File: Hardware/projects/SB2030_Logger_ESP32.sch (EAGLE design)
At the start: 91 parts, among them IC1 MPU6050, T2 S8050, T3 S8050, T4 S8050, U1 ESP32-WROOM-32E, U2 TJA1051T/3, U3 AMS1117-5.0, U4 AMS1117-3.3, U5 SN65C1168PWR, X1 1751280

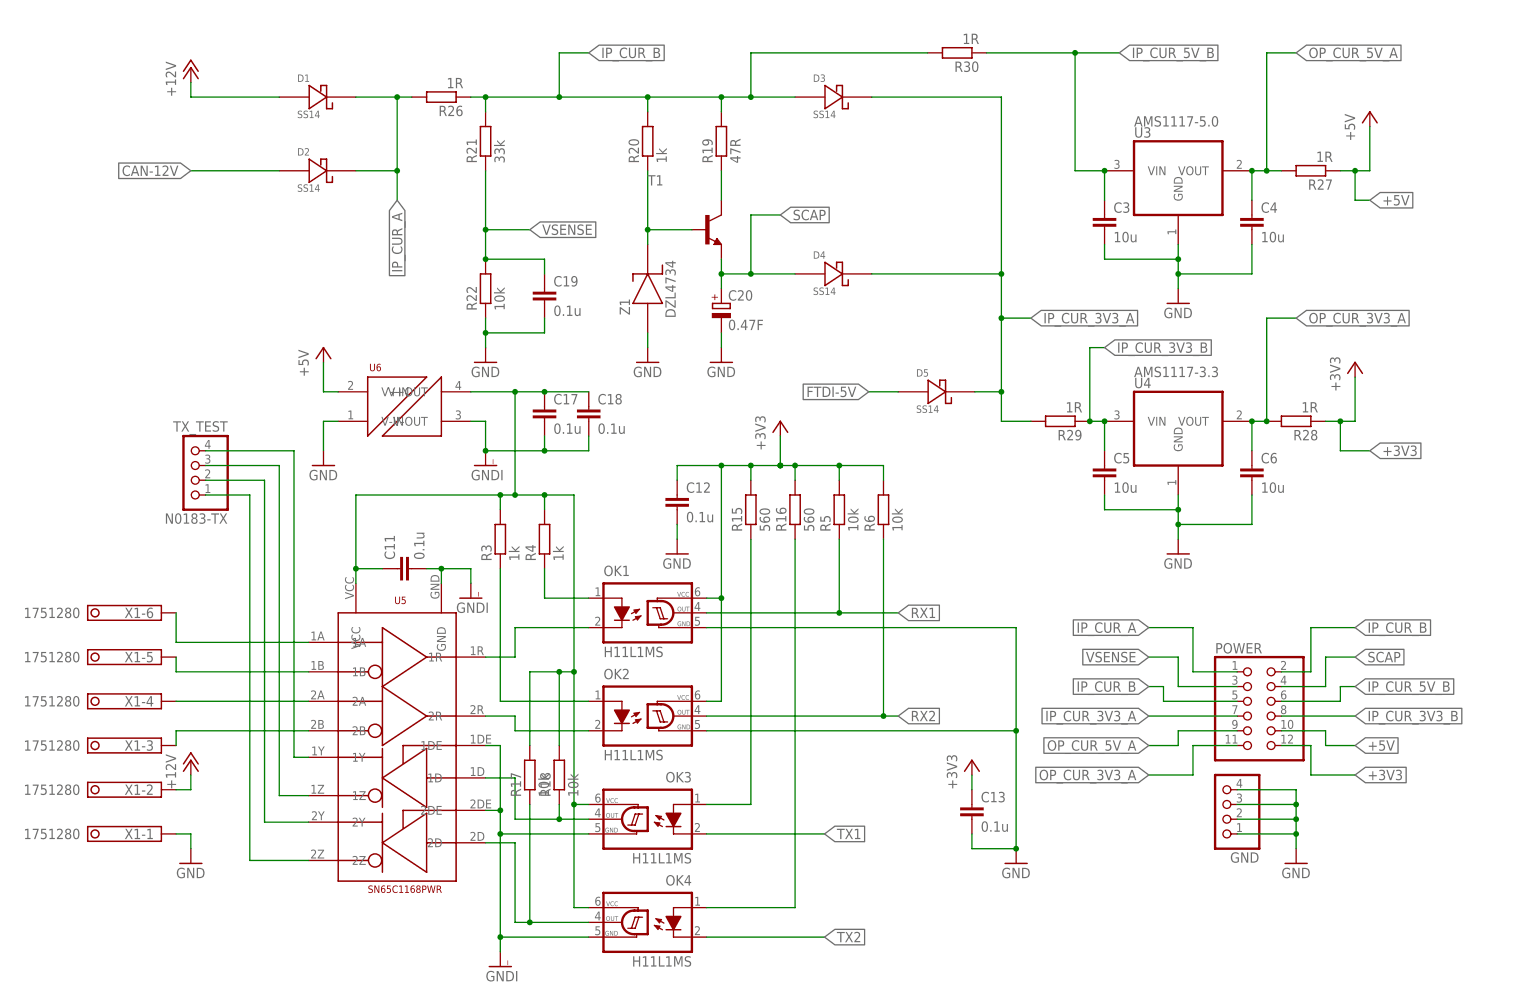
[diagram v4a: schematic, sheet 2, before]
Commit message: Updates to logger schematic and board layout.
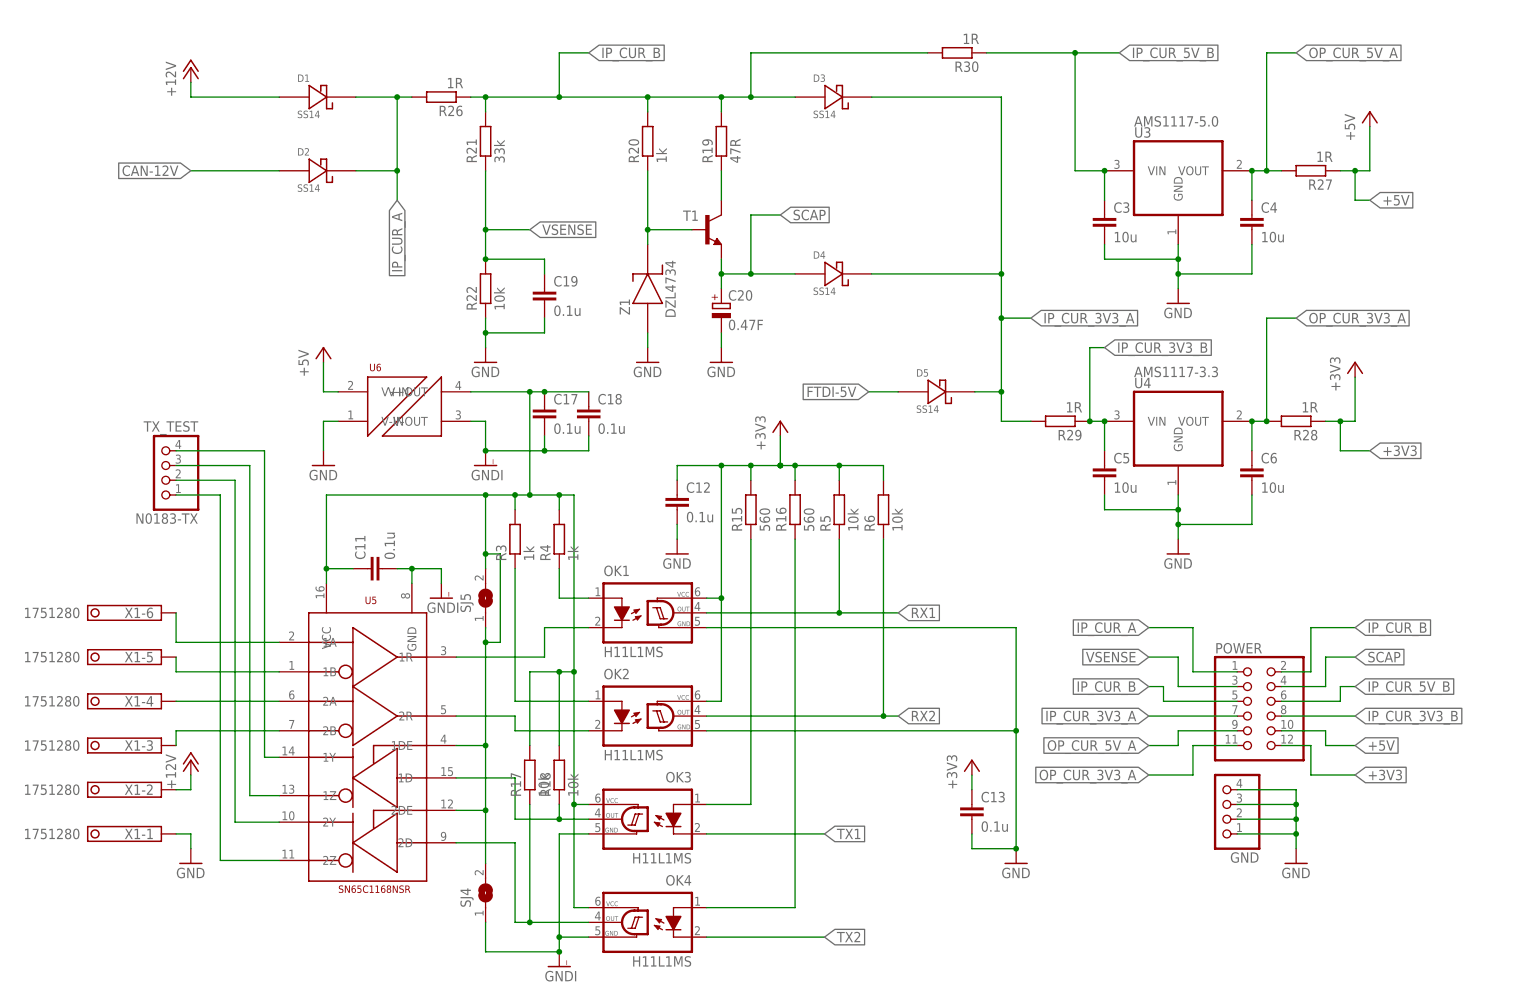
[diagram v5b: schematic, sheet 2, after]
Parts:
- removed SJ2, SJ3: (no value), jumper:SJ
- added C21: 10u, rcl:C-EUC0805
- added C22: 0.1u, rcl:C-EUC0805
- added SJ4, SJ5: (no value), jumper:SJ
- U5: value SN65C1168PWR -> SN65C1168NSR
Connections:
- net +3V3: now also C21.1, C22.1
- net GND: now also C21.2, C22.2
- net GNDI: now also SJ4.1; no longer U5.1DE, U5.2DE
- net N$10: no longer SJ3.1, SJ3.2
- net N$21: now also SJ4.2, SJ5.1, SJ5.2, U5.1DE, U5.2DE
- net N$22: no longer SJ2.1, SJ2.2
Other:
- moved on the sheet: C11, N0183-TX, R3, R4, U5

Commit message: Updates to design for WIBL, board and schematic, to match new SMPS integration, and other small fixes for layout of power input, and super-capacitor charging circuit.
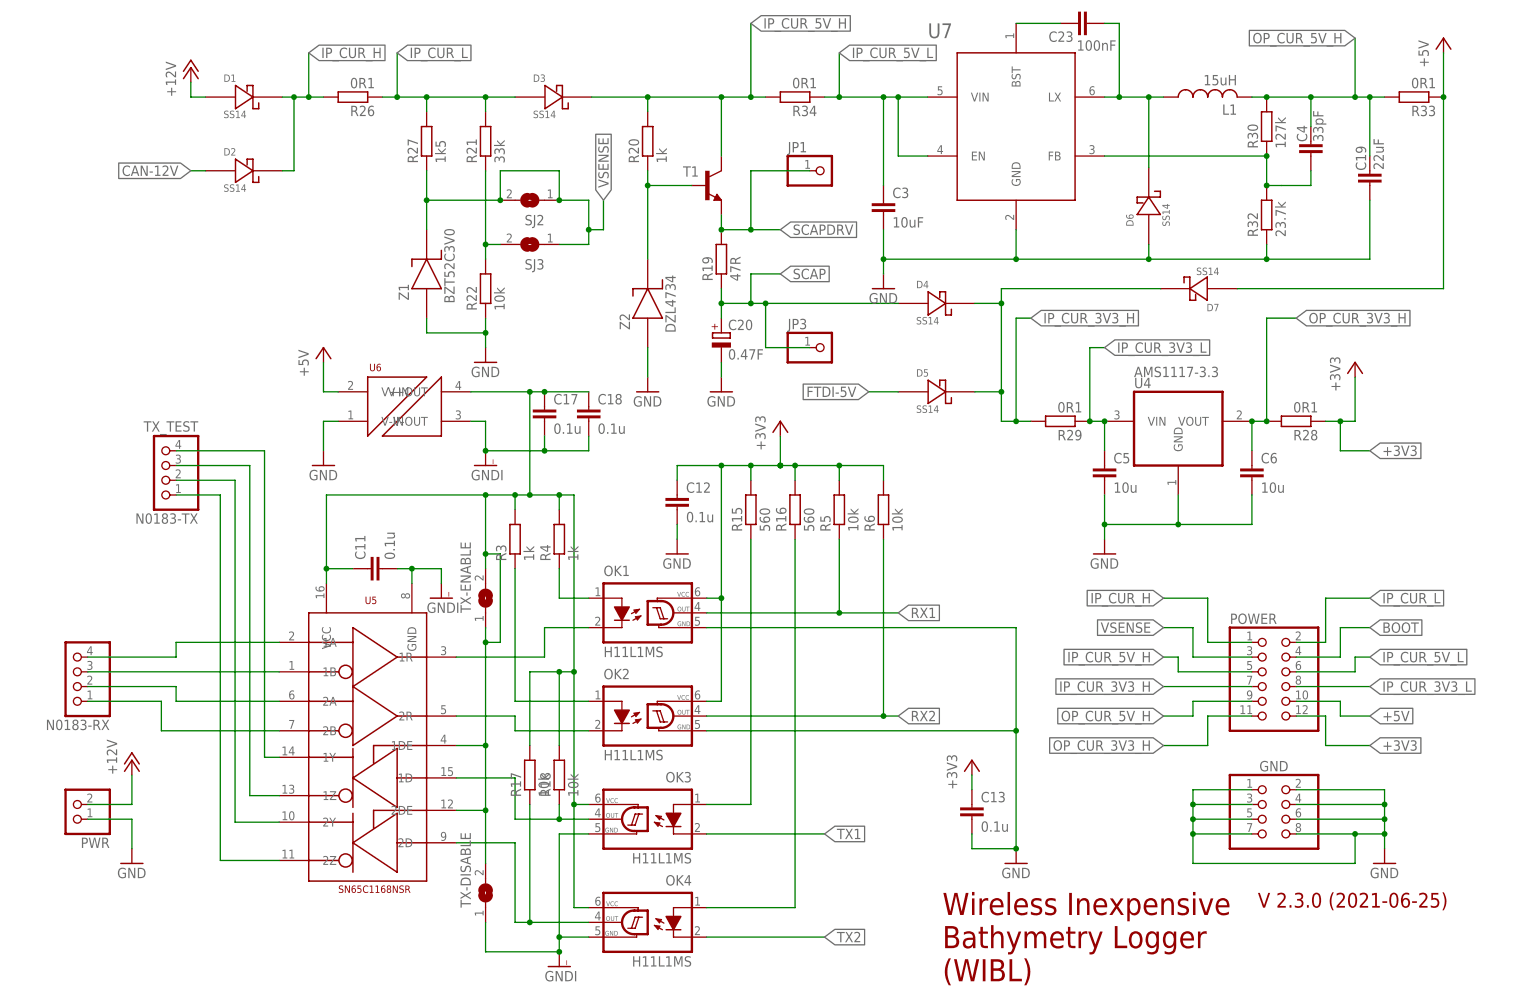
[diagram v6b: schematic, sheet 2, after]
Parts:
- removed C8: 0.1u, rcl:C-EUC0805
- removed U3: AMS1117-5.0, burr-brown:REG1117
- removed X1: 1751280, con-phoenix-350:1751280
- added C23: 100nF, sb2030_logger:C0402
- added D6, D7: SS14, sb2030_logger:SS14
- added JP1, JP3: (no value), pinhead:PINHD-1X1
- added L1: 15uH, sb2030_logger:MWSA0603S
- added N0183-RX: (no value), pinhead:PINHD-1X4
- added PWR: (no value), pinhead:PINHD-1X2
- added R32: 23.7k, rcl:R-EU_R0603
- added R33, R34: 0R1, rcl:R-EU_R0603
- added R35: 47k, rcl:R-EU_R0805
- added SJ2, SJ3: (no value), jumper:SJ
- added U7: (no value), sb2030_logger:BL9352A
- added Z2: DZL4734, sb2030_logger:DZL4734
- C19: value 0.1u -> 22uF; device rcl:C-EUC0805 -> rcl:C-EUC0603
- C3: value 10u -> 10uF; device rcl:C-EUC0805 -> rcl:C-EUC1206
- C4: value 10u -> 33pF; device rcl:C-EUC0805 -> rcl:C-EUC0603
- C7: value 0.1u -> 1uF
- GND: device pinhead:PINHD-1X4 -> pinhead:PINHD-2X4
- R26, R28, R29: value 1R -> 0R1; device rcl:R-EU_R0805 -> rcl:R-EU_R0603
- R27: value 1R -> 1k5
- R30: value 1R -> 127k; device rcl:R-EU_R0805 -> rcl:R-EU_R0603
- Z1: value DZL4734 -> BZT52C3V0; device sb2030_logger:DZL4734 -> sb2030_logger:BZT52C3V0
- renumbered SJ4 to TX-DISABLE, SJ5 to TX-ENABLE
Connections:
- net IP_CUR_3V3_B renamed IP_CUR_3V3_L
- net IP_CUR_A renamed IP_CUR_H
- net OP_CUR_3V3_A renamed OP_CUR_3V3_H
- removed net IP_CUR_3V3_A: D3.K, D4.K, D5.K, POWER.7, R29.2
- removed net IP_CUR_5V_B: C3.1, POWER.6, R30.1, U3.VIN
- removed net IP_CUR_B: D3.A, POWER.2, POWER.5, R19.2, R20.2, R21.2, R26.1, R30.2
- removed net N$12: C8.1, T2.C, U1.GPIO0/BOOT
- removed net OP_CUR_5V_A: C4.1, POWER.9, R27.2, U3.VOUT
- new net BOOT: POWER.4, T2.C, U1.GPIO0/BOOT
- new net IP_CUR_3V3_H: D4.K, D5.K, D7.K, POWER.7, R29.2
- new net IP_CUR_5V_H: D3.K, POWER.5, R20.2, R34.2, T1.C
- new net IP_CUR_5V_L: C3.1, POWER.6, R34.1, U7.EN, U7.VIN
- new net IP_CUR_L: D3.A, POWER.2, R21.2, R26.1, R27.2
- new net N$45: C23.2, D6.K, L1.1, U7.LX
- new net N$46: R21.1, R22.2, SJ3.2
- new net N$48: C4.1, R30.1, R32.2, U7.FB
- new net OP_CUR_5V_H: C19.2, C4.2, L1.2, POWER.9, R30.2, R33.2
- new net SCAPDRV: JP1.1, R19.2, T1.E
- net +12V: now also PWR.2; no longer X1-2.K
- net +5V: now also D7.A, R33.1; no longer R27.1
- net GND: now also C19.1, D6.A, GND.5, GND.6, GND.7, GND.8, PWR.1, R32.1, R35.1, U7.GND, Z2.A; no longer C19.2, C4.2, C8.2, U3.GND, X1-1.K
- net N$17: now also N0183-RX.4; no longer X1-6.K
- net N$18: now also N0183-RX.3; no longer X1-5.K
- net N$19: now also N0183-RX.2; no longer X1-4.K
- net N$20: now also N0183-RX.1; no longer X1-3.K
- net N$37: now also R35.2
- net N$41: now also Z2.K; no longer Z1.K
- net N$42: now also C23.1, U7.BST; no longer R19.1, T1.C
- net SCAP: now also JP3.1, R19.1; no longer POWER.4, T1.E
- net VSENSE: now also R27.1, SJ2.1, SJ2.2, SJ3.1, Z1.K; no longer C19.1, R21.1, R22.2
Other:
- note added: "V 2.3.0 (2021-06-25)"
- note added: "V2.3.0 (2021-06-25)"
- note added: "Wireless Inexpensive Bathymetry Logger (WIBL)"
- moved on the sheet: C19, C20, C3, C4, D1, D2, D3, D4, POWER, R19, R26, R27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

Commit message: Please enter the commit message for your changes. Lines starting
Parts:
- removed C14: 2n2, rcl:C-EUC0805
- removed C15: 0.1u, rcl:C-EUC0805
- removed C16: 10n, rcl:C-EUC0805
- removed IC1: MPU6050, invensense:MPU6050
- added C8: 0.1u, rcl:C-EUC0805
- added R36: 10k, rcl:R-EU_R0805
- added U3: LSM6DS3TR-C, LSM6DS3TR-C:LSM6DS3TR-C
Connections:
- removed net N$23: C14.1, IC1G$1.CPOUT
- removed net N$5: I2C.2, IC1G$1.SCL, R7.1, U1.GPIO22/SCL
- removed net N$8: I2C.1, IC1G$1.SDA, R8.1, U1.GPIO21/SDA
- removed net N$9: C15.1, IC1G$1.REGOUT
- new net INT1: R8.1, U1.GPI37/S-VN, U3.INT1
- new net SCL: I2C.1, R7.1, U1.GPIO21/SDA, U3.SDA
- new net SDA: I2C.2, R36.1, U1.GPIO22/SCL, U3.SCL
- net +3V3: now also C8.1, R36.2, U3.CS, U3.SCX, U3.SDX, U3.VDD, U3.VDDIO; no longer C16.1, IC1G$1.VDD, IC1G$1.VLOGIC
- net GND: now also C8.2, U3.GND, U3.SDO/SA0; no longer C14.2, C15.2, C16.2, IC1G$1.AD0, IC1G$1.CLKIN, IC1G$1.FSYNC, IC1G$1.GND, IC1G$1.GND@1
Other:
- moved on the sheet: R7, R8
